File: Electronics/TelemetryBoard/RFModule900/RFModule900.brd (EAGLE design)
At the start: 100 x 80 mm, 34 parts

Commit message: more work on the RF 900mhz module
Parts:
- added C21: 1pF, SparkFun-Capacitors:0402-CAP
- added C22, C23: 3pF, SparkFun-Capacitors:0402-CAP
- added C24, C25: 4.3pF, SparkFun-Capacitors:0402-CAP
- added C26, C27, C28: 56pF, SparkFun-Capacitors:0402-CAP
- added C29: 3.9pF, SparkFun-Capacitors:0402-CAP
- added C30: 5.6pF, SparkFun-Capacitors:0402-CAP
- added C31: 22pF, SparkFun-Capacitors:0402-CAP
- added C32: 1uF, SparkFun-Capacitors:EIA3216
- added C34: 33pF, SparkFun-Capacitors:0402-CAP
- added C35: 100pF, SparkFun-Capacitors:0402-CAP
- added C36: 100nF, SparkFun-Capacitors:0402-CAP
- added C37: 2.2uF, SparkFun-Capacitors:0402-CAP
- added L10: 12nH, SparkFun-Passives:C0402
- added L11: 10nH, SparkFun-Passives:C0402
- added L6: 18nH, SparkFun-Passives:C0402
- added L7: 22nH, SparkFun-Passives:C0402
- added L8: 8.2nH, SparkFun-Passives:C0402
- added L9: 100nH, SparkFun-Passives:C0402
- added R5, R6, R7: 5k, SparkFun-Resistors:0402-RES
- added SJ2: JUMPER-PAD-3-2OF3_NC_BY_TRACE_SMALL, SparkFun-Passives:PAD-JUMPER-3-2OF3_NC_BY_TRACE_YES_SILK_FULL_BOX
- added Y1: 30 Mhz, RitLaunchInitiative:4-SMD_3.2_X_2.5
- C1: value 7.5pF -> 2.7pF
- C11: value 1uF -> 10uF
- C16: value 10uF -> 1uF
- C19: value 1uF -> 22pF
- C2: value 39pF -> 1uF
- C8: value 39pF -> 22pF
- L1: value 2.7nH -> 10nH
- L4, L5: value BLM15HB121SN1 -> (none)
- moved C19 134.7 mm to (-45.7, -96.5)
- moved R4 126.0 mm to (-38.1, -85.1)
- moved C8 122.2 mm to (-45.7, -92.7)
- moved C16 120.3 mm to (-38.1, -81.3)
- moved R1 119.1 mm to (-34.3, -77.5)
- moved C11 111.5 mm to (-38.1, -77.5)
- moved C10 107.8 mm to (-34.3, -73.7)
- moved C2 105.4 mm to (-38.1, -73.7)
- moved L1 95.3 mm to (-38.1, -58.4)
- moved C1 90.2 mm to (-38.1, -66.0)
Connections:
- removed net N$2 (its old number): C1.2, U$2.P$6
- new net 3V1: C32.A, U$4.5
- new net 5V: R5.1, U$4.1
- new net N$12: C21.1, L6.1, U$1.P$2
- new net N$13: C21.2, C23.2, L7.2
- new net N$14: C23.1, C28.2
- new net N$15: C25.2, L8.2, X1.ANTENNA
- new net N$16: C26.2, U$3.P$7
- new net N$19: C11.1, C2.1, R1.1
- new net N$20: C29.1, L9.2, U$1.P$4
- new net N$21: C29.2, L10.1
- new net N$22: C30.2, L1.1, L10.2
- new net N$23: C27.1, U$3.P$2
- new net N$24: C28.1, U$3.P$11
- new net N$25: R6.1, SJ2.2
- new net N$26: C19.2, R6.2, U$3.P$15
- new net N$27: C22.2, L6.2, L7.1, U$1.P$3
- new net N$28: U$1.P$17, Y1.P$1
- new net N$29: U$1.P$16, Y1.P$3
- new net N$4: C16.1, R4.2, U$2.P$23
- new net RADIO_ENABLE: R7.2, U$1.P$1
- new net TR_SWITCH_CTL: C31.2, U$1.P$20, U$3.P$14
- net 3.3V: now also C34.2, C35.2, C36.2, C37.2, C8.2, L9.1, SJ2.3, U$1.P$6, U$1.P$8, U$3.P$16
- net GND: now also C1.1, C16.2, C19.1, C2.2, C22.1, C24.1, C25.1, C30.1, C31.1, C32.C, C34.1, C35.1, C36.1, C37.1, C8.1, R7.1, SJ2.1, U$1.GND_PAD, U$1.P$18, U$3.P$1, U$3.P$10, U$3.P$12, U$3.P$13, U$3.P$3, U$3.P$4, U$3.P$5, U$3.P$6, U$3.P$8, U$3.P$9, U$3.P$GNDPAD, U$4.2; no longer C16.1, C19.2, L1.2
- net N$1: now also C1.2, L1.2, L11.1; no longer C1.1, C2.2, L1.1
- net N$10: now also C24.2, C26.1, L8.1; no longer U$3.P$7, X1.ANTENNA
- net N$17: now also L11.2, U$2.P$6; no longer C19.1, R4.2, U$2.P$23
- net N$3: now also C12.1, C17.1, R2.1; no longer C2.1
- net N$5: now also C27.2; no longer C8.2
- net N$7: now also R5.2, U$4.3; no longer C11.1, C12.1, C16.2, C17.1, R1.1, R2.1

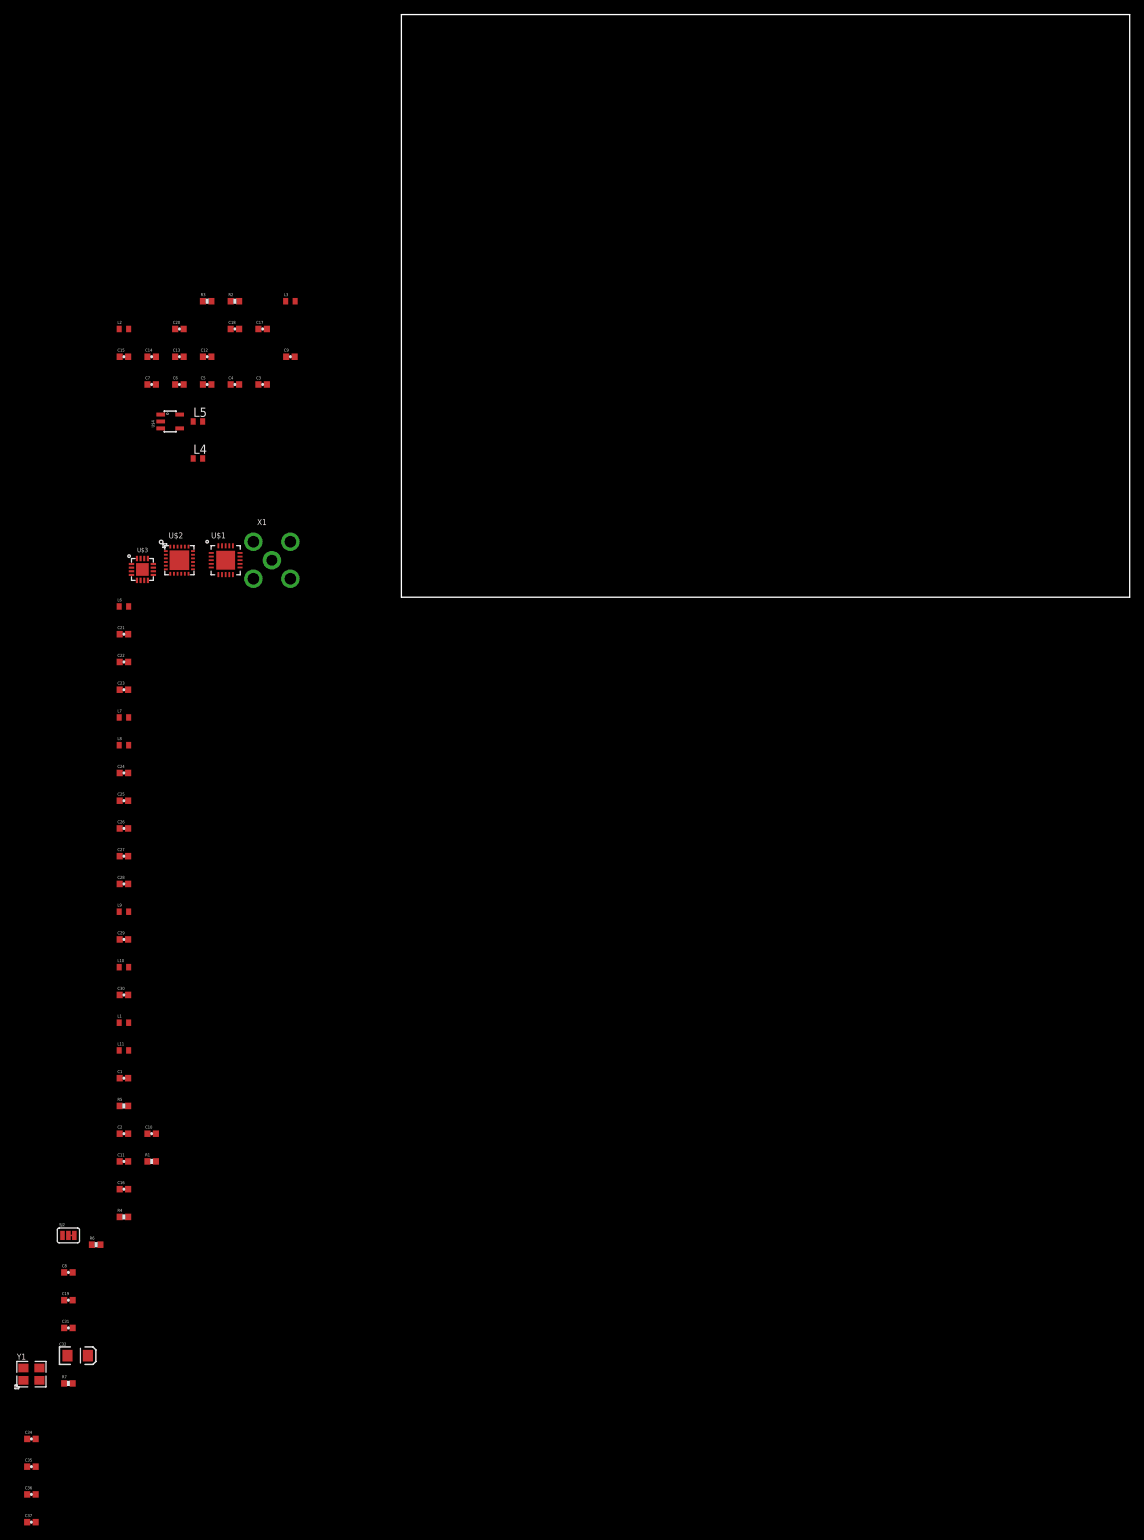
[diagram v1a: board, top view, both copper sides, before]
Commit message: adding status leds and power sequencing as well as clean up
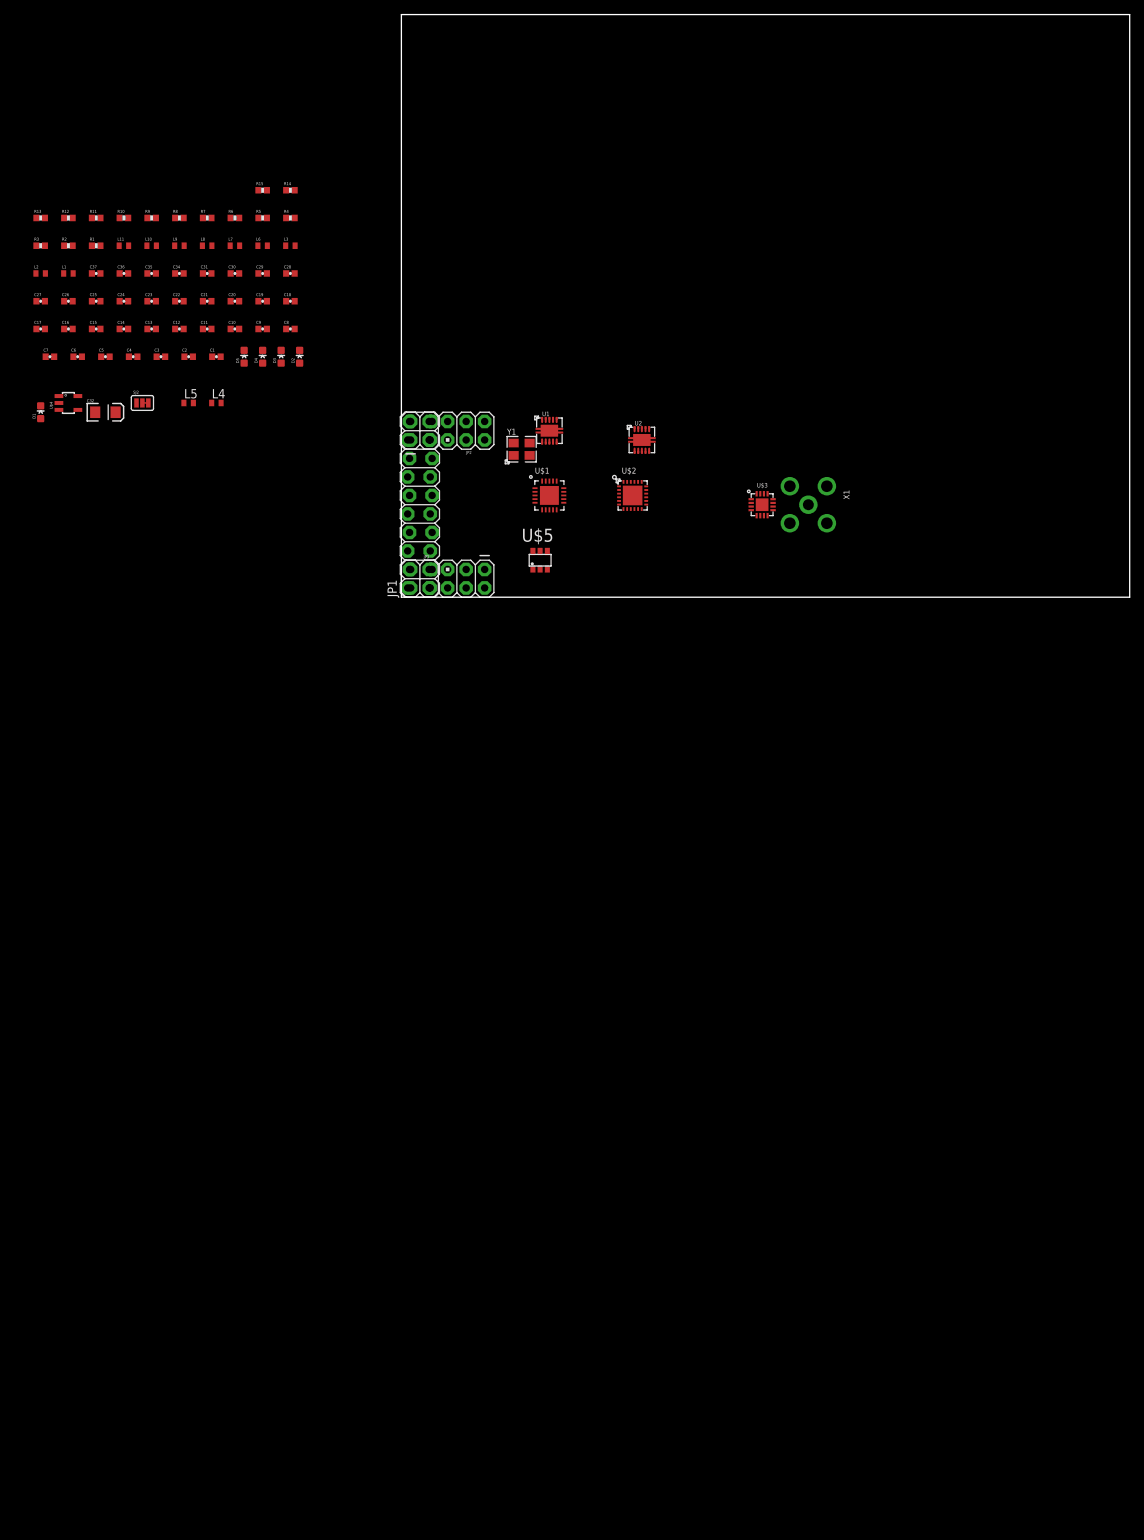
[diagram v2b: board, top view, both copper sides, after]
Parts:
- added D1, D2, D3, D4, D5: (no value), SparkFun-LED:LED-0603
- added JP1: (no value), SparkFun-Connectors:2X10_LOCK_SPECIAL
- added JP2, JP3: (no value), SparkFun-Connectors:AVR_ICSP
- added R10, R11, R12, R14, R15, R8, R9: 5k, SparkFun-Resistors:0402-RES
- added R13: 10k, SparkFun-Resistors:0402-RES
- added U$5: AO6602, RitLaunchInitiative:TSOP-6
- added U1, U2: TPS2561, RitLaunchInitiative:10-VFDFN
- SJ2: value JUMPER-PAD-3-2OF3_NC_BY_TRACE_SMALL -> invert Control Signal
- moved C37 171.7 mm to (-41.9, 44.5)
- moved C36 168.1 mm to (-38.1, 44.5)
- moved C35 164.7 mm to (-34.3, 44.5)
- moved C34 161.3 mm to (-30.5, 44.5)
- moved R7 161.1 mm to (-26.7, 52.1)
- moved C31 146.0 mm to (-26.7, 44.5)
- moved Y1 143.7 mm to (16.5, 20.3)
- moved R6 142.3 mm to (-22.9, 52.1)
- moved C19 139.7 mm to (-19.1, 40.6)
- moved R4 139.1 mm to (-15.2, 52.1)
- moved C8 133.1 mm to (-15.2, 36.8)
- moved C32 129.6 mm to (-40.6, 25.4)
- moved R1 126.0 mm to (-41.9, 48.3)
- moved R5 123.4 mm to (-19.1, 52.1)
- moved C16 118.4 mm to (-45.7, 36.8)
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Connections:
- new net 3V3_MAIN: R13.2
- new net GPIO0: U$1.P$9
- new net GPIO1: U$1.P$10
- new net GPIO2: U$1.P$19
- new net N$11: R9.2, U1.P$7
- new net N$30: D2.C, R10.2
- new net N$31: D1.C, R12.2
- new net N$32: R8.2, U2.P$7
- new net N$33: D5.A, R5.2
- new net N$34: D5.C, U$5.6
- new net N$35: D4.A, U$5.2
- new net N$36: D4.C, R15.1
- new net N_IRQ: JP1.11, U$1.P$11
- new net N_SEL: JP1.19, U$1.P$15
- new net PA_3V3: C14.2, C15.1, C20.1, D2.A, L4.2, L5.2, R3.1, R4.1, U$2.P$1, U$2.P$2, U$2.P$22, U$2.P$3, U2.P$8, U2.P$9
- new net PA_ENABLE: JP1.20, U$4.3, U2.P$4, U2.P$5
- new net PA_TEMP: JP1.14, R13.1, R14.2
- new net RADIO_3V3: C34.2, C35.2, C36.2, C37.2, D1.A, L9.1, U$1.P$6, U$1.P$8, U1.P$9
- new net SCLK: JP1.13, U$1.P$12
- new net SDI: JP1.17, U$1.P$14
- new net SDO: JP1.15, U$1.P$13
- new net STATUS_LED: JP1.16
- net 3.3V: now also JP1.1, JP1.2, JP1.3, JP1.4, JP1.6, R5.1, U$5.4, U1.P$2, U1.P$3, U2.P$2, U2.P$3; no longer C14.2, C15.1, C20.1, C34.2, C35.2, C36.2, C37.2, L4.2, L5.2, L9.1, R3.1, R4.1, U$1.P$6, U$1.P$8, U$2.P$1, U$2.P$2, U$2.P$22, U$2.P$3
- net 3V1: now also D3.A
- net 5V: now also JP1.9; no longer R5.1
- net GND: now also JP1.10, JP1.12, JP1.5, JP1.7, JP1.8, R10.1, R11.1, R12.1, R14.1, R15.2, R8.1, R9.1, U$5.5, U1.GNDPAD, U1.P$1, U2.GNDPAD, U2.P$1, Y1.P$2, Y1.P$4
- net N$7: now also D3.C, R11.2; no longer R5.2, U$4.3
- net RADIO_ENABLE: now also JP1.18, U1.P$4
- net TR_SWITCH_CTL: now also U$5.1, U$5.3

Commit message: Cleaning more things up
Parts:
- added R16, R17: 10k, SparkFun-Resistors:0402-RES
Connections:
- net GND: now also R16.2
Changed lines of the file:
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@@
 <element name="JP2" library="SparkFun-Connectors" package="AVR_ICSP" value="" x="6.35" y="22.86" rot="R90"/>
 <element name="JP3" library="SparkFun-Connectors" package="AVR_ICSP" value="" x="6.35" y="2.54" rot="R270"/>
+<element name="R16" library="SparkFun-Resistors" package="0402-RES" value="10k" x="-49.53" y="-3.81"/>
+<element name="R17" library="SparkFun-Resistors" package="0402-RES" value="10k" x="-49.53" y="-7.62"/>
 </elements>
 <signals>
@@
 <contactref element="U$5" pad="5"/>
 <contactref element="R15" pad="2"/>
+<contactref element="R16" pad="2"/>
 <wire x1="58.42" y1="10.16" x2="58.42" y2="15.24" width="0" layer="19" extent="1-1"/>
 <wire x1="53.34" y1="15.24" x2="58.42" y2="15.24" width="0" layer="19" extent="1-1"/>
@@
 <wire x1="33.02" y1="21.59" x2="31.75" y2="13.97" width="0" layer="19" extent="1-1"/>
 <wire x1="32.02" y1="23.065" x2="33.02" y2="21.59" width="0" layer="19" extent="1-1"/>
-<wire x1="20.32" y1="22.86" x2="32.02" y2="23.065" width="0" layer="19" extent="1-1"/>
+<wire x1="20.32" y1="13.97" x2="31.75" y2="13.97" width="0" layer="19" extent="1-1"/>
+<wire x1="20.32" y1="15.945" x2="20.32" y2="13.97" width="0" layer="19" extent="1-1"/>
+<wire x1="17.61" y1="19.47" x2="20.32" y2="15.945" width="0" layer="19" extent="1-1"/>
+<wire x1="15.41" y1="21.17" x2="17.61" y2="19.47" width="0" layer="19" extent="1-1"/>
+<wire x1="20.32" y1="22.86" x2="17.61" y2="19.47" width="0" layer="19" extent="1-1"/>
 <wire x1="19.32" y1="24.335" x2="20.32" y2="22.86" width="0" layer="19" extent="1-1"/>
-<wire x1="17.61" y1="19.47" x2="20.32" y2="22.86" width="0" layer="19" extent="1-1"/>
-<wire x1="15.41" y1="21.17" x2="17.61" y2="19.47" width="0" layer="19" extent="1-1"/>
-<wire x1="20.32" y1="15.945" x2="17.61" y2="19.47" width="0" layer="19" extent="1-1"/>
-<wire x1="20.32" y1="13.97" x2="20.32" y2="15.945" width="0" layer="19" extent="1-1"/>
 <wire x1="19.05" y1="6.28" x2="20.32" y2="13.97" width="0" layer="19" extent="1-1"/>
 <wire x1="4.2164" y1="8.89" x2="19.05" y2="6.28" width="0" layer="19" extent="1-1"/>
@@
 <wire x1="-18.47" y1="55.88" x2="-27.25" y2="52.07" width="0" layer="19" extent="1-1"/>
 <wire x1="-15.82" y1="55.88" x2="-18.47" y2="55.88" width="0" layer="19" extent="1-1"/>
+<wire x1="-48.95" y1="-3.81" x2="-42.04" y2="25.4" width="0" layer="19" extent="1-1"/>
 </signal>
 <signal name="N$5">
